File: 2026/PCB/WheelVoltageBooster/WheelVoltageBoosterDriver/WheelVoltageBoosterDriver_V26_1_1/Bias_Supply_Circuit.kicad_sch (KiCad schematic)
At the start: 33 parts, among them U5 MAX20405AFOA/VY+, U6 LD1117DT33CTR, U7 MAX20405AFOA/VY+

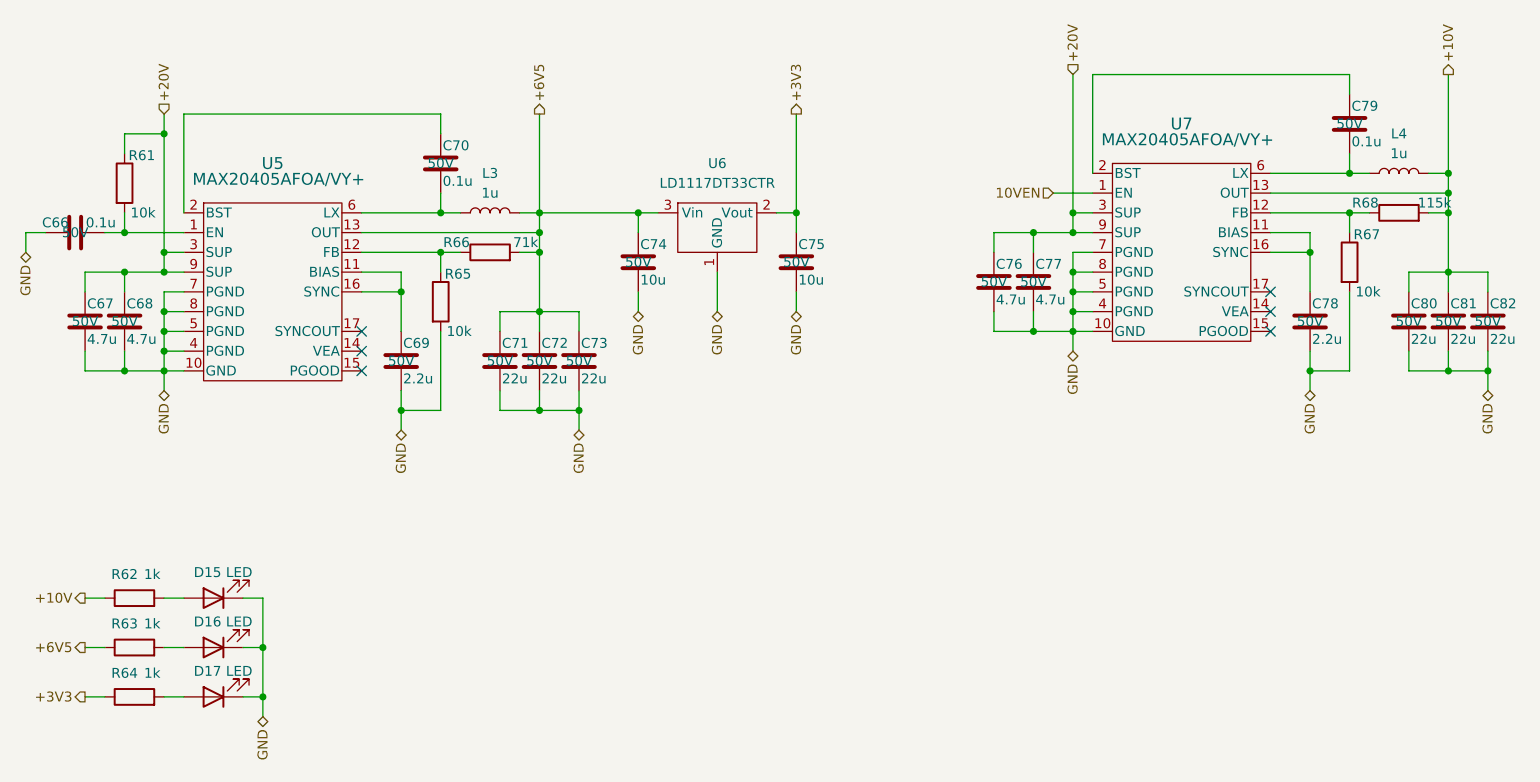
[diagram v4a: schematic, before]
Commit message: インダクタ再選定＆安全率縮小
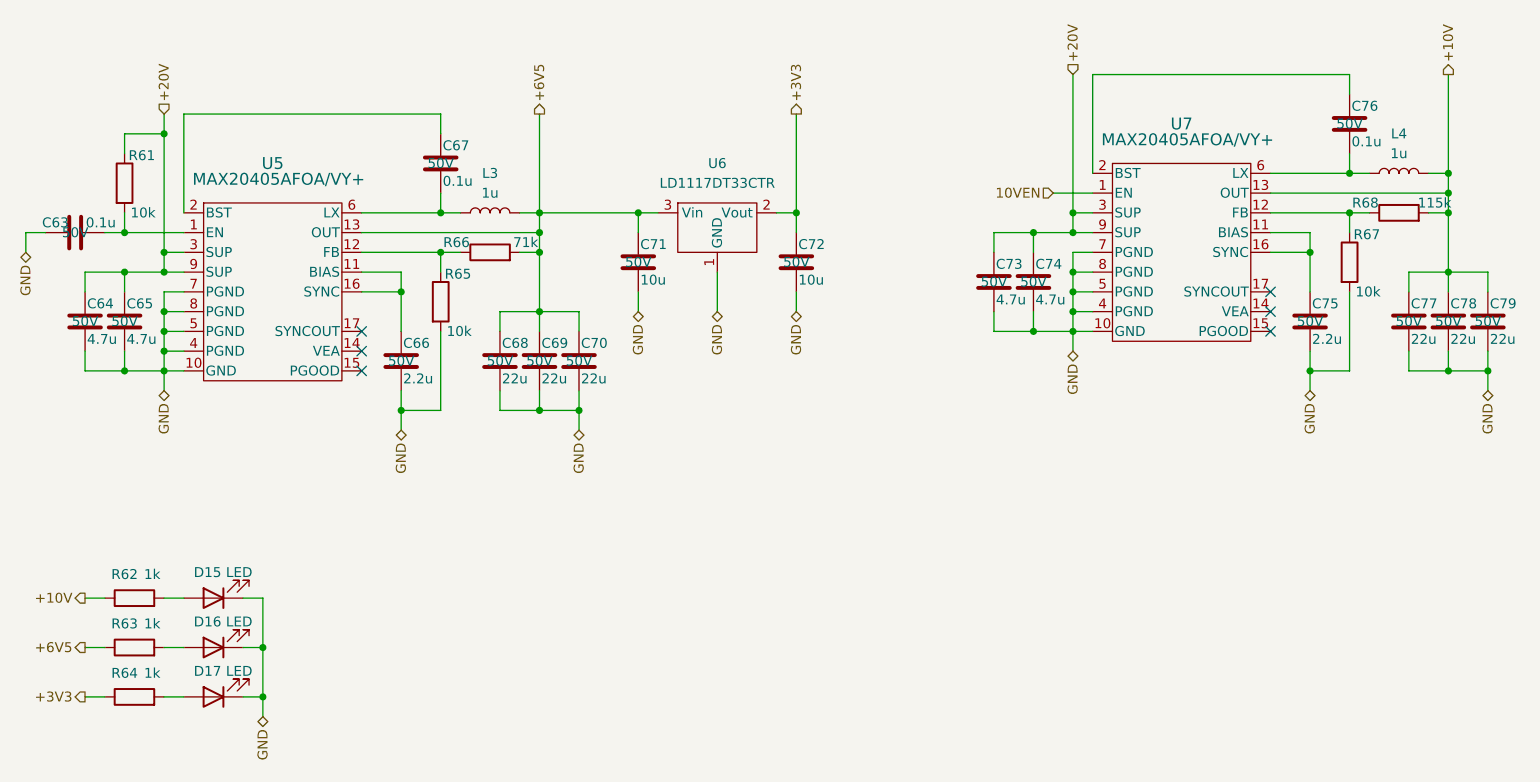
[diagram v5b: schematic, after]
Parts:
- renumbered C66 to C63, C67 to C64, C68 to C65, C69 to C66, C70 to C67, C71 to C68, C72 to C69, C73 to C70, C74 to C71, C75 to C72, C76 to C73, C77 to C74, C78 to C75, C79 to C76, C80 to C77, C81 to C78, C82 to C79
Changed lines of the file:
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@@
 		(on_board yes)
 		(dnp no)
-		(property "Reference" "C69"
+		(property "Reference" "C66"
 			(at 92.964 100.584 0)
 			(effects
@@
 			(project "WheelVoltageBoosterDriver_V26_1_1"
 				(path "/80c9ed4f-d051-48b1-8382-19040773b73e/6c235b48-13ab-434e-8894-09a09ebdd0ec"
-					(reference "C69")
+					(reference "C66")
 					(unit 1)
 				)
@@
 		(on_board yes)
 		(dnp no)
-		(property "Reference" "C72"
+		(property "Reference" "C69"
 			(at 110.744 100.584 0)
 			(effects
@@
 			(project "WheelVoltageBoosterDriver_V26_1_1"
 				(path "/80c9ed4f-d051-48b1-8382-19040773b73e/6c235b48-13ab-434e-8894-09a09ebdd0ec"
-					(reference "C72")
+					(reference "C69")
 					(unit 1)
 				)
@@
 		(on_board yes)
 		(dnp no)
-		(property "Reference" "C80"
+		(property "Reference" "C77"
 			(at 222.504 95.504 0)
 			(effects
@@
 			(project "WheelVoltageBoosterDriver_V26_1_1"
 				(path "/80c9ed4f-d051-48b1-8382-19040773b73e/6c235b48-13ab-434e-8894-09a09ebdd0ec"
-					(reference "C80")
+					(reference "C77")
 					(unit 1)
 				)
@@
 		(on_board yes)
 		(dnp no)
-		(property "Reference" "C74"
+		(property "Reference" "C71"
 			(at 123.444 87.884 0)
 			(effects
@@
 			(project "WheelVoltageBoosterDriver_V26_1_1"
 				(path "/80c9ed4f-d051-48b1-8382-19040773b73e/6c235b48-13ab-434e-8894-09a09ebdd0ec"
-					(reference "C74")
+					(reference "C71")
 					(unit 1)
 				)
@@
 		(on_board yes)
 		(dnp no)
-		(property "Reference" "C66"
+		(property "Reference" "C63"
 			(at 48.26 85.09 90)
 			(effects
@@
 			(project "WheelVoltageBoosterDriver_V26_1_1"
 				(path "/80c9ed4f-d051-48b1-8382-19040773b73e/6c235b48-13ab-434e-8894-09a09ebdd0ec"
-					(reference "C66")
+					(reference "C63")
 					(unit 1)
 				)
@@
 		(on_board yes)
 		(dnp no)
-		(property "Reference" "C68"
+		(property "Reference" "C65"
 			(at 57.404 95.504 0)
 			(effects
@@
 			(project "WheelVoltageBoosterDriver_V26_1_1"
 				(path "/80c9ed4f-d051-48b1-8382-19040773b73e/6c235b48-13ab-434e-8894-09a09ebdd0ec"
-					(reference "C68")
+					(reference "C65")
 					(unit 1)
 				)
@@
 		(on_board yes)
 		(dnp no)
-		(property "Reference" "C79"
+		(property "Reference" "C76"
 			(at 214.884 70.104 0)
 			(effects
@@
 			(project "WheelVoltageBoosterDriver_V26_1_1"
 				(path "/80c9ed4f-d051-48b1-8382-19040773b73e/6c235b48-13ab-434e-8894-09a09ebdd0ec"
-					(reference "C79")
+					(reference "C76")
 					(unit 1)
 				)
@@
 		(on_board yes)
 		(dnp no)
-		(property "Reference" "C73"
+		(property "Reference" "C70"
 			(at 115.824 100.584 0)
 			(effects
@@
 			(project "WheelVoltageBoosterDriver_V26_1_1"
 				(path "/80c9ed4f-d051-48b1-8382-19040773b73e/6c235b48-13ab-434e-8894-09a09ebdd0ec"
-					(reference "C73")
+					(reference "C70")
 					(unit 1)
 				)
@@
 		(on_board yes)
 		(dnp no)
-		(property "Reference" "C81"
+		(property "Reference" "C78"
 			(at 227.584 95.504 0)
 			(effects
@@
 			(project "WheelVoltageBoosterDriver_V26_1_1"
 				(path "/80c9ed4f-d051-48b1-8382-19040773b73e/6c235b48-13ab-434e-8894-09a09ebdd0ec"
-					(reference "C81")
+					(reference "C78")
 					(unit 1)
 				)
@@
 		(on_board yes)
 		(dnp no)
-		(property "Reference" "C77"
+		(property "Reference" "C74"
 			(at 174.244 90.424 0)
 			(effects
@@
 			(project "WheelVoltageBoosterDriver_V26_1_1"
 				(path "/80c9ed4f-d051-48b1-8382-19040773b73e/6c235b48-13ab-434e-8894-09a09ebdd0ec"
-					(reference "C77")
+					(reference "C74")
 					(unit 1)
 				)
@@
 		(on_board yes)
 		(dnp no)
-		(property "Reference" "C75"
+		(property "Reference" "C72"
 			(at 143.764 87.884 0)
 			(effects
@@
 			(project "WheelVoltageBoosterDriver_V26_1_1"
 				(path "/80c9ed4f-d051-48b1-8382-19040773b73e/6c235b48-13ab-434e-8894-09a09ebdd0ec"
-					(reference "C75")
+					(reference "C72")
 					(unit 1)
 				)
@@
 		(on_board yes)
 		(dnp no)
-		(property "Reference" "C71"
+		(property "Reference" "C68"
 			(at 105.664 100.584 0)
 			(effects
@@
 			(project "WheelVoltageBoosterDriver_V26_1_1"
 				(path "/80c9ed4f-d051-48b1-8382-19040773b73e/6c235b48-13ab-434e-8894-09a09ebdd0ec"
-					(reference "C71")
+					(reference "C68")
 					(unit 1)
 				)
@@
 		(on_board yes)
 		(dnp no)
-		(property "Reference" "C70"
+		(property "Reference" "C67"
 			(at 98.044 75.184 0)
 			(effects
@@
 			(project "WheelVoltageBoosterDriver_V26_1_1"
 				(path "/80c9ed4f-d051-48b1-8382-19040773b73e/6c235b48-13ab-434e-8894-09a09ebdd0ec"
-					(reference "C70")
+					(reference "C67")
 					(unit 1)
 				)
@@
 		(on_board yes)
 		(dnp no)
-		(property "Reference" "C78"
+		(property "Reference" "C75"
 			(at 209.804 95.504 0)
 			(effects
@@
 			(project "WheelVoltageBoosterDriver_V26_1_1"
 				(path "/80c9ed4f-d051-48b1-8382-19040773b73e/6c235b48-13ab-434e-8894-09a09ebdd0ec"
-					(reference "C78")
+					(reference "C75")
 					(unit 1)
 				)
@@
 		(on_board yes)
 		(dnp no)
-		(property "Reference" "C82"
+		(property "Reference" "C79"
 			(at 232.664 95.504 0)
 			(effects
@@
 			(project "WheelVoltageBoosterDriver_V26_1_1"
 				(path "/80c9ed4f-d051-48b1-8382-19040773b73e/6c235b48-13ab-434e-8894-09a09ebdd0ec"
-					(reference "C82")
+					(reference "C79")
 					(unit 1)
 				)
@@
 		(on_board yes)
 		(dnp no)
-		(property "Reference" "C67"
+		(property "Reference" "C64"
 			(at 52.324 95.504 0)
 			(effects
@@
 			(project "WheelVoltageBoosterDriver_V26_1_1"
 				(path "/80c9ed4f-d051-48b1-8382-19040773b73e/6c235b48-13ab-434e-8894-09a09ebdd0ec"
-					(reference "C67")
+					(reference "C64")
 					(unit 1)
 				)
@@
 		(on_board yes)
 		(dnp no)
-		(property "Reference" "C76"
+		(property "Reference" "C73"
 			(at 169.164 90.424 0)
 			(effects
@@
 			(project "WheelVoltageBoosterDriver_V26_1_1"
 				(path "/80c9ed4f-d051-48b1-8382-19040773b73e/6c235b48-13ab-434e-8894-09a09ebdd0ec"
-					(reference "C76")
-					(unit 1)
-				)
+					(reference "C73")
+					(unit 1)
+				)

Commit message: 部品配置完了
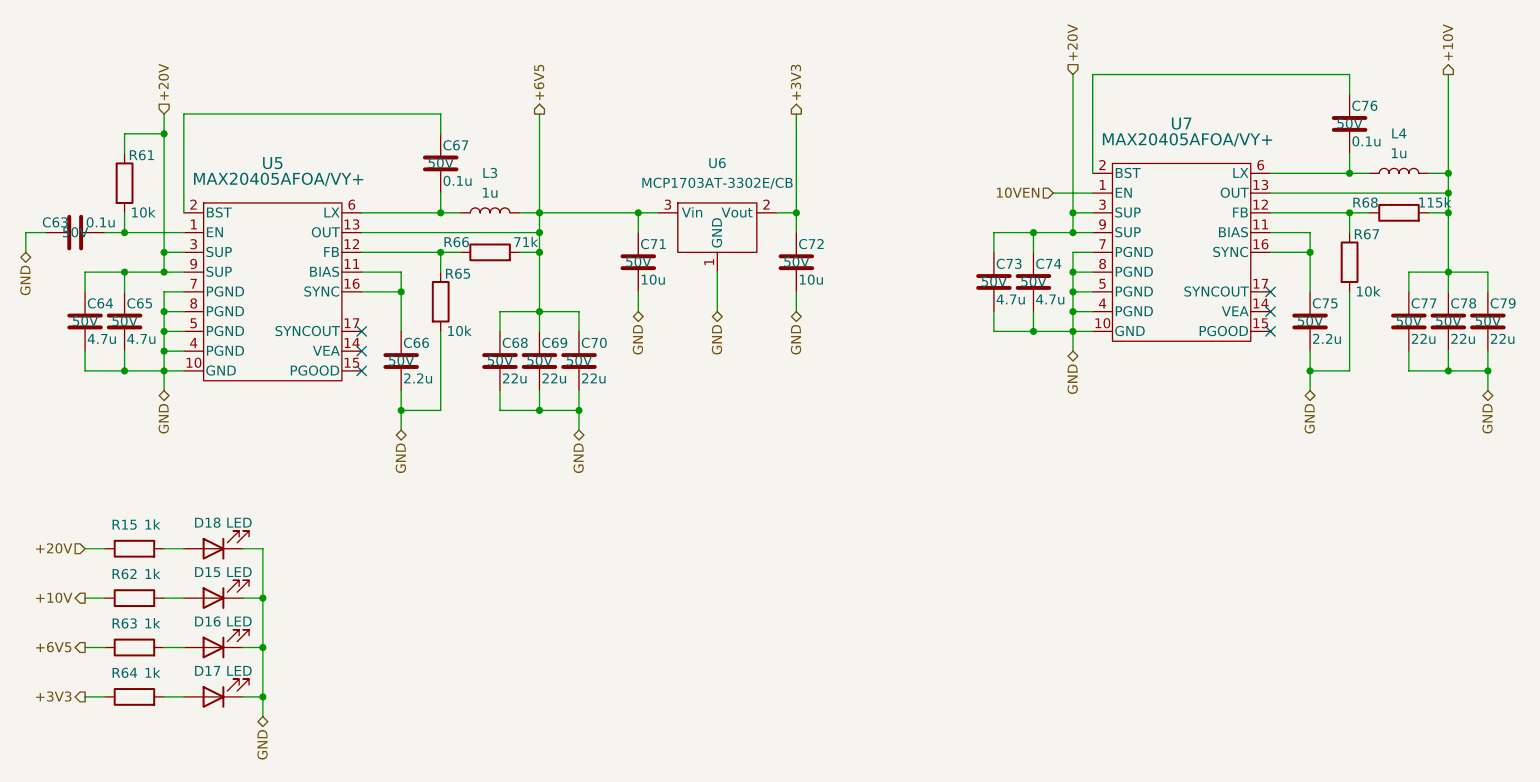
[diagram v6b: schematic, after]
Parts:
- removed U6: LD1117DT33CTR, Package_TO_SOT_SMD:TO-252-2, symbol WheelVoltageBooster_LIB_SYM:LD1117DT33CTR
- added D18: LED, WheelVoltageBooster_LIB_FTP:LED_1608_user_dif, symbol Device:LED
- added R15: 1k, Resistor_SMD:R_0603_1608Metric_Pad0.98x0.95mm_HandSolder, symbol Device:R
- added U6: MCP1703AT-3302E/CB, Package_TO_SOT_SMD:TSOT-23, symbol WheelVoltageBooster_LIB_SYM:MCP1703AT-3302E/CB
- R62, R63, R64: footprint Resistor_SMD:R_0402_1005Metric_Pad0.72x0.64mm_HandSolder -> Resistor_SMD:R_0603_1608Metric_Pad0.98x0.95mm_HandSolder
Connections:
- net +20V: now also R15.1
- net +3V3: now also U6.2 (Vout)
- net +6V5: now also U6.3 (Vin)
- net GND: now also D18.1 (K), U6.1 (GND)
- new net: D18.2 (A), R15.2
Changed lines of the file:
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@@
 	)
 	(junction
+		(at 74.93 133.35)
+		(diameter 0)
+		(color 0 0 0 0)
+	)
+	(junction
 		(at 209.55 88.9)
 		(diameter 0)
@@
 	(wire
 		(pts
+			(xy 72.39 127) (xy 74.93 127)
+		)
+		(stroke
+			(width 0)
+			(type default)
+		)
+	)
+	(wire
+		(pts
 			(xy 173.99 99.06) (xy 179.07 99.06)
 		)
@@
 	(wire
 		(pts
+			(xy 74.93 127) (xy 74.93 133.35)
+		)
+		(stroke
+			(width 0)
+			(type default)
+		)
+	)
+	(wire
+		(pts
 			(xy 232.41 104.14) (xy 232.41 106.68)
 		)
@@
 	(wire
 		(pts
+			(xy 52.07 127) (xy 54.61 127)
+		)
+		(stroke
+			(width 0)
+			(type default)
+		)
+	)
+	(wire
+		(pts
 			(xy 179.07 83.82) (xy 179.07 86.36)
 		)
@@
 	(wire
 		(pts
+			(xy 62.23 127) (xy 64.77 127)
+		)
+		(stroke
+			(width 0)
+			(type default)
+		)
+	)
+	(wire
+		(pts
 			(xy 224.79 83.82) (xy 227.33 83.82)
 		)
@@
 	(hierarchical_label "+20V"
 		(shape input)
+		(at 52.07 127 180)
+		(effects
+			(font
+				(size 1.27 1.27)
+			)
+			(justify right)
+		)
+	)
+	(hierarchical_label "+20V"
+		(shape input)
 		(at 179.07 66.04 90)
 		(effects
@@
 	)
 	(symbol
-		(lib_id "Device:L")
-		(at 104.14 83.82 90)
+		(lib_id "WheelVoltageBooster_LIB_SYM:MCP1703AT-3302E/CB")
+		(at 133.35 80.01 0)
 		(unit 1)
 		(exclude_from_sim no)
@@
 		(dnp no)
 		(fields_autoplaced yes)
-		(property "Reference" "L3"
-			(at 104.14 78.74 90)
+		(property "Reference" "U6"
+			(at 133.35 77.47 0)
 			(effects
 				(font
@@
 			)
 		)
-		(property "Value" "1u"
-			(at 104.14 81.28 90)
+		(property "Value" "MCP1703AT-3302E/CB"
+			(at 133.35 80.01 0)
 			(effects
 				(font
@@
 			)
 		)
-		(property "Footprint" "WheelVoltageBooster_LIB_FTP:74438366010"
-			(at 104.14 83.82 0)
+		(property "Footprint" "Package_TO_SOT_SMD:TSOT-23"
+			(at 133.35 80.01 0)
 			(effects
 				(font
@@
 			)
 		)
-		(property "Datasheet" "~"
-			(at 104.14 83.82 0)
+		(property "Datasheet" ""
+			(at 133.35 80.01 0)
 			(effects
 				(font
@@
 			)
 		)
-		(property "Description" "Inductor"
-			(at 104.14 83.82 0)
+		(property "Description" ""
+			(at 133.35 80.01 0)
 			(effects
 				(font
@@
 			)
 		)
+		(pin "3"
+		)
+		(pin "1"
+		)
 		(pin "1"
 		)
@@
 		)
 		(instances
-			(project "WheelVoltageBoosterDriver_V26_1_1"
+			(project ""
 				(path "/80c9ed4f-d051-48b1-8382-19040773b73e/6c235b48-13ab-434e-8894-09a09ebdd0ec"
-					(reference "L3")
+					(reference "U6")
 					(unit 1)
 				)
@@
 	)
 	(symbol
-		(lib_id "Device:R")
-		(at 58.42 133.35 90)
+		(lib_id "Device:L")
+		(at 104.14 83.82 90)
 		(unit 1)
 		(exclude_from_sim no)
@@
 		(on_board yes)
 		(dnp no)
-		(property "Reference" "R62"
-			(at 57.15 130.302 90)
+		(fields_autoplaced yes)
+		(property "Reference" "L3"
+			(at 104.14 78.74 90)
 			(effects
 				(font
@@
 			)
 		)
-		(property "Value" "1k"
-			(at 60.706 130.302 90)
+		(property "Value" "1u"
+			(at 104.14 81.28 90)
 			(effects
 				(font
@@
 			)
 		)
-		(property "Footprint" "Resistor_SMD:R_0402_1005Metric_Pad0.72x0.64mm_HandSolder"
-			(at 58.42 135.128 90)
+		(property "Footprint" "WheelVoltageBooster_LIB_FTP:74438366010"
+			(at 104.14 83.82 0)
 			(effects
 				(font
@@
 		)
 		(property "Datasheet" "~"
-			(at 58.42 133.35 0)
+			(at 104.14 83.82 0)
 			(effects
 				(font
@@
 			)
 		)
-		(property "Description" "Resistor"
-			(at 58.42 133.35 0)
+		(property "Description" "Inductor"
+			(at 104.14 83.82 0)
 			(effects
 				(font
@@
 			(project "WheelVoltageBoosterDriver_V26_1_1"
 				(path "/80c9ed4f-d051-48b1-8382-19040773b73e/6c235b48-13ab-434e-8894-09a09ebdd0ec"
-					(reference "R62")
+					(reference "L3")
 					(unit 1)
 				)
@@
 	)
 	(symbol
-		(lib_id "WheelVoltageBooster_LIB_SYM:LD1117DT33CTR")
-		(at 133.35 80.01 0)
+		(lib_id "Device:R")
+		(at 58.42 133.35 90)
 		(unit 1)
 		(exclude_from_sim no)
@@
 		(on_board yes)
 		(dnp no)
-		(fields_autoplaced yes)
-		(property "Reference" "U6"
-			(at 133.35 77.47 0)
+		(property "Reference" "R62"
+			(at 57.15 130.302 90)
 			(effects
 				(font
@@
 			)
 		)
-		(property "Value" "LD1117DT33CTR"
-			(at 133.35 80.01 0)
+		(property "Value" "1k"
+			(at 60.706 130.302 90)
 			(effects
 				(font
@@
 			)
 		)
-		(property "Footprint" "Package_TO_SOT_SMD:TO-252-2"
-			(at 133.35 80.01 0)
+		(property "Footprint" "Resistor_SMD:R_0603_1608Metric_Pad0.98x0.95mm_HandSolder"
+			(at 58.42 135.128 90)
 			(effects
 				(font
@@
 			)
 		)
-		(property "Datasheet" ""
-			(at 133.35 80.01 0)
+		(property "Datasheet" "~"
+			(at 58.42 133.35 0)
 			(effects
 				(font
@@
 			)
 		)
-		(property "Description" ""
-			(at 133.35 80.01 0)
+		(property "Description" "Resistor"
+			(at 58.42 133.35 0)
 			(effects
 				(font
@@
 		(pin "1"
 		)
-		(pin "3"
-		)
 		(pin "2"
 		)
-		(pin "1"
-		)
 		(instances
 			(project "WheelVoltageBoosterDriver_V26_1_1"
 				(path "/80c9ed4f-d051-48b1-8382-19040773b73e/6c235b48-13ab-434e-8894-09a09ebdd0ec"
-					(reference "U6")
+					(reference "R62")
 					(unit 1)
 				)
@@
 			)
 		)
-		(property "Footprint" "Resistor_SMD:R_0402_1005Metric_Pad0.72x0.64mm_HandSolder"
+		(property "Footprint" "Resistor_SMD:R_0603_1608Metric_Pad0.98x0.95mm_HandSolder"
 			(at 58.42 141.478 90)
 			(effects
@@
 	)
 	(symbol
+		(lib_id "Device:LED")
+		(at 68.58 127 180)
+		(unit 1)
+		(exclude_from_sim no)
+		(in_bom yes)
+		(on_board yes)
+		(dnp no)
+		(property "Reference" "D18"
+			(at 67.818 123.698 0)
+			(effects
+				(font
+					(size 1.27 1.27)
+				)
+			)
+		)
+		(property "Value" "LED"
+			(at 71.882 123.698 0)
+			(effects
+				(font
+					(size 1.27 1.27)
+				)
+			)
+		)
+		(property "Footprint" "WheelVoltageBooster_LIB_FTP:LED_1608_user_dif"
+			(at 68.58 127 0)
+			(effects
+				(font
+					(size 1.27 1.27)
+				)
+				(hide yes)
+			)
+		)
+		(property "Datasheet" "~"
+			(at 68.58 127 0)
+			(effects
+				(font
+					(size 1.27 1.27)
+				)
+				(hide yes)
+			)
+		)
+		(property "Description" "Light emitting diode"
+			(at 68.58 127 0)
+			(effects
+				(font
+					(size 1.27 1.27)
+				)
+				(hide yes)
+			)
+		)
+		(pin "1"
+		)
+		(pin "2"
+		)
+		(instances
+			(project "WheelVoltageBoosterDriver_V26_1_1"
+				(path "/80c9ed4f-d051-48b1-8382-19040773b73e/6c235b48-13ab-434e-8894-09a09ebdd0ec"
+					(reference "D18")
+					(unit 1)
+				)
+			)
+		)
+	)
+	(symbol
 		(lib_id "Device:R")
 		(at 58.42 146.05 90)
@@
 			)
 		)
-		(property "Footprint" "Resistor_SMD:R_0402_1005Metric_Pad0.72x0.64mm_HandSolder"
+		(property "Footprint" "Resistor_SMD:R_0603_1608Metric_Pad0.98x0.95mm_HandSolder"
 			(at 58.42 147.828 90)
 			(effects
@@
 					(unit 1)
 				)
+			)
+		)
+	)
+	(symbol
+		(lib_id "Device:R")
+		(at 58.42 127 90)
+		(unit 1)
+		(exclude_from_sim no)
+		(in_bom yes)
+		(on_board yes)
+		(dnp no)
+		(property "Reference" "R15"
+			(at 57.15 123.952 90)
+			(effects
+				(font
+					(size 1.27 1.27)
+				)
+			)
+		)
+		(property "Value" "1k"
+			(at 60.706 123.952 90)
+			(effects
+				(font
+					(size 1.27 1.27)
+				)
+			)
+		)
+		(property "Footprint" "Resistor_SMD:R_0603_1608Metric_Pad0.98x0.95mm_HandSolder"
+			(at 58.42 128.778 90)
+			(effects
+				(font
+					(size 1.27 1.27)
+				)
+				(hide yes)
+			)
+		)
+		(property "Datasheet" "~"
+			(at 58.42 127 0)
+			(effects
+				(font
+					(size 1.27 1.27)
+				)
+				(hide yes)
+			)
+		)
+		(property "Description" "Resistor"
+			(at 58.42 127 0)
+			(effects
+				(font
+					(size 1.27 1.27)
+				)
+				(hide yes)
+			)
+		)
+		(pin "1"
+		)
+		(pin "2"
+		)
+		(instances
+			(project "WheelVoltageBoosterDriver_V26_1_1"
+				(path "/80c9ed4f-d051-48b1-8382-19040773b73e/6c235b48-13ab-434e-8894-09a09ebdd0ec"
+					(reference "R15")
+					(unit 1)
+				)

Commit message: 製造ファイル出力
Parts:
- R15: value 1k -> 50k
- R62: value 1k -> 10k
- R63: value 1k -> 4.7k
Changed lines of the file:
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@@
 			)
 		)
-		(property "Value" "1k"
+		(property "Value" "10k"
 			(at 60.706 130.302 90)
 			(effects
@@
 			)
 		)
-		(property "Value" "1k"
+		(property "Value" "4.7k"
 			(at 60.706 136.652 90)
 			(effects
@@
 			)
 		)
-		(property "Value" "1k"
+		(property "Value" "50k"
 			(at 60.706 123.952 90)
 			(effects
